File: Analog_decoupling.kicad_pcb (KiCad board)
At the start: 2 copper layers, 188.1 x 142 mm, 0 parts

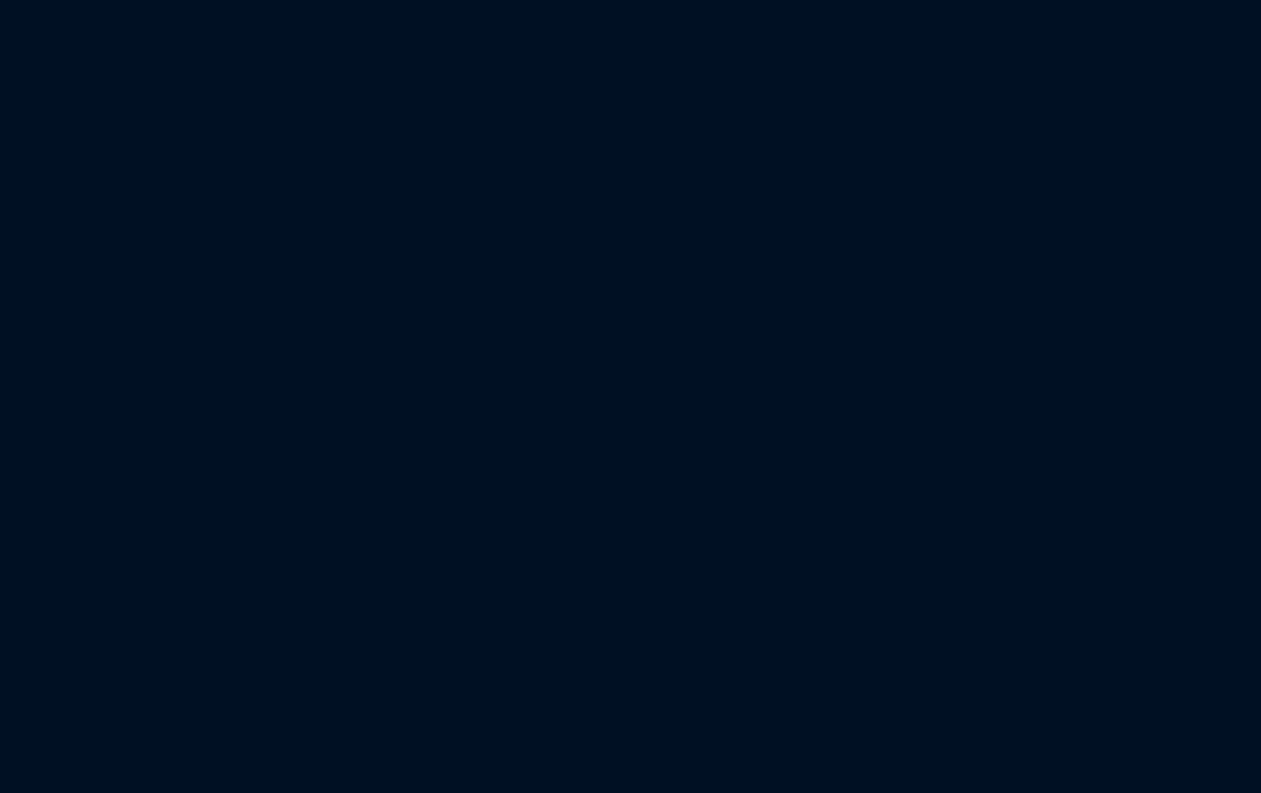
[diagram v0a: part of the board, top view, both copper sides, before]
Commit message: Analog decoupling elements place to PCB
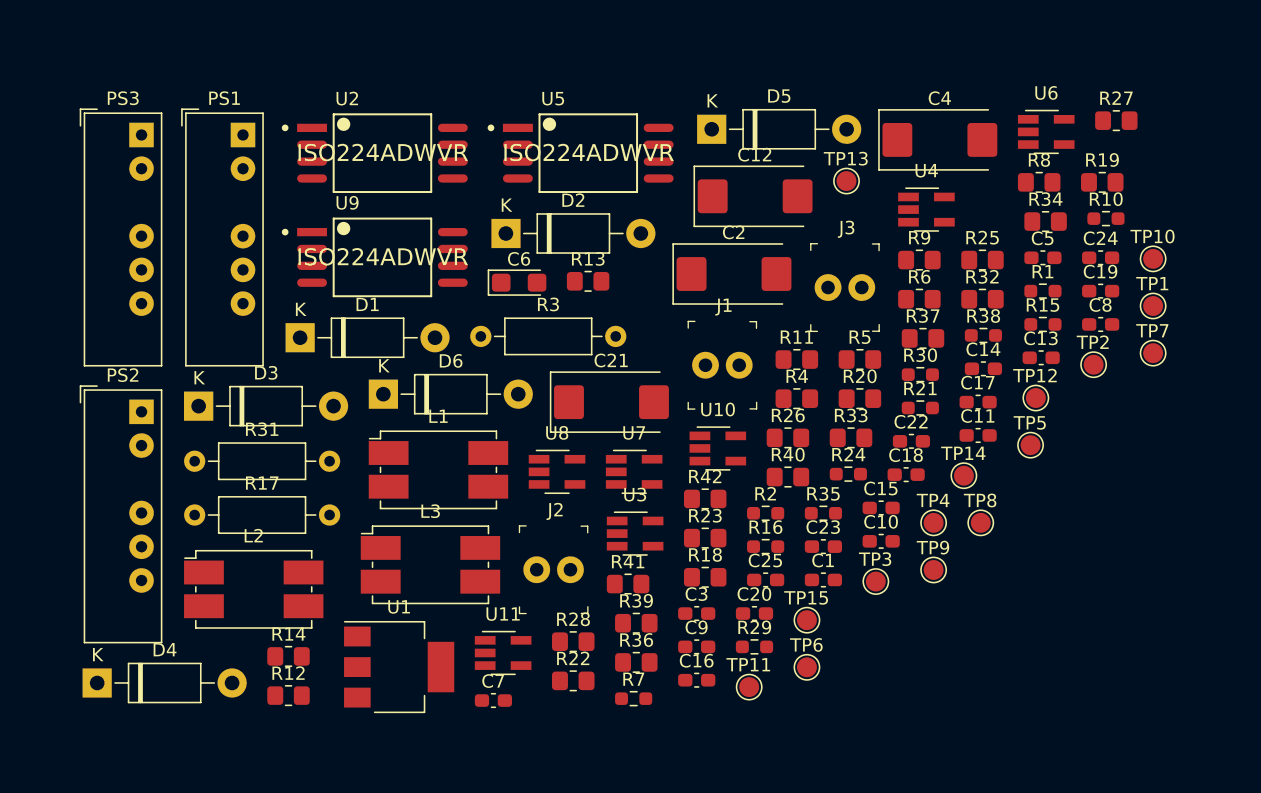
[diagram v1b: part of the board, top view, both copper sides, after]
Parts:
- added C1: 1µF, Capacitor_SMD:C_0603_1608Metric_Pad1.08x0.95mm_HandSolder, F.Cu at (167.9, 128.7)
- added C10: 1µF, Capacitor_SMD:C_0603_1608Metric_Pad1.08x0.95mm_HandSolder, F.Cu at (172.2, 125.8)
- added C11: 1µF, Capacitor_SMD:C_0603_1608Metric_Pad1.08x0.95mm_HandSolder, F.Cu at (179.5, 117.8)
- added C12: 10µFx35, Capacitor_Tantalum_SMD:CP_EIA-7343-30_AVX-N_Pad2.25x2.55mm_HandSolder, F.Cu at (162.7, 99.8)
- added C13: 1µF, Capacitor_SMD:C_0603_1608Metric_Pad1.08x0.95mm_HandSolder, F.Cu at (184.3, 112.0)
- added C14: 0.1µF, Capacitor_SMD:C_0603_1608Metric_Pad1.08x0.95mm_HandSolder, F.Cu at (179.9, 112.8)
- added C15: 0.22µF, Capacitor_SMD:C_0603_1608Metric_Pad1.08x0.95mm_HandSolder, F.Cu at (172.2, 123.3)
- added C16: 330pF, Capacitor_SMD:C_0603_1608Metric_Pad1.08x0.95mm_HandSolder, F.Cu at (158.3, 136.3)
- added C17: 1µF, Capacitor_SMD:C_0603_1608Metric_Pad1.08x0.95mm_HandSolder, F.Cu at (179.5, 115.3)
- added C18: 1µF, Capacitor_SMD:C_0603_1608Metric_Pad1.08x0.95mm_HandSolder, F.Cu at (174.1, 120.8)
- added C19: 1µF, Capacitor_SMD:C_0603_1608Metric_Pad1.08x0.95mm_HandSolder, F.Cu at (188.7, 107.0)
- added C2: 10µFx35, Capacitor_Tantalum_SMD:CP_EIA-7343-30_AVX-N_Pad2.25x2.55mm_HandSolder, F.Cu at (161.1, 105.7)
- added C20: 1µF, Capacitor_SMD:C_0603_1608Metric_Pad1.08x0.95mm_HandSolder, F.Cu at (162.7, 131.2)
- added C21: 10µFx35, Capacitor_Tantalum_SMD:CP_EIA-7343-30_AVX-N_Pad2.25x2.55mm_HandSolder, F.Cu at (151.9, 115.3)
- added C22: 1µF, Capacitor_SMD:C_0603_1608Metric_Pad1.08x0.95mm_HandSolder, F.Cu at (174.5, 118.3)
- added C23: 0.1µF, Capacitor_SMD:C_0603_1608Metric_Pad1.08x0.95mm_HandSolder, F.Cu at (167.9, 126.2)
- added C24: 0.22µF, Capacitor_SMD:C_0603_1608Metric_Pad1.08x0.95mm_HandSolder, F.Cu at (188.7, 104.5)
- added C25: 330pF, Capacitor_SMD:C_0603_1608Metric_Pad1.08x0.95mm_HandSolder, F.Cu at (163.5, 128.7)
- added C3: 1µF, Capacitor_SMD:C_0603_1608Metric_Pad1.08x0.95mm_HandSolder, F.Cu at (158.3, 131.2)
- added C4: 10µFx35, Capacitor_Tantalum_SMD:CP_EIA-7343-30_AVX-N_Pad2.25x2.55mm_HandSolder, F.Cu at (176.6, 95.6)
- added C5: 1µF, Capacitor_SMD:C_0603_1608Metric_Pad1.08x0.95mm_HandSolder, F.Cu at (184.4, 104.5)
- added C6: 10µFx16, Capacitor_Tantalum_SMD:CP_EIA-3216-10_Kemet-I, F.Cu at (144.9, 106.3)
- added C7: 0.1µF, Capacitor_SMD:C_0603_1608Metric_Pad1.08x0.95mm_HandSolder, F.Cu at (143.0, 137.8)
- added C8: 0.22µF, Capacitor_SMD:C_0603_1608Metric_Pad1.08x0.95mm_HandSolder, F.Cu at (188.7, 109.5)
- added C9: 330pF, Capacitor_SMD:C_0603_1608Metric_Pad1.08x0.95mm_HandSolder, F.Cu at (158.3, 133.8)
- added D1: 1N4743A, Diode_THT:D_DO-41_SOD81_P10.16mm_Horizontal, F.Cu at (128.4, 110.5)
- added D2: 1N4743A, Diode_THT:D_DO-41_SOD81_P10.16mm_Horizontal, F.Cu at (143.9, 102.6)
- added D3: 1N4743A, Diode_THT:D_DO-41_SOD81_P10.16mm_Horizontal, F.Cu at (120.8, 115.6)
- added D4: 1N4743A, Diode_THT:D_DO-41_SOD81_P10.16mm_Horizontal, F.Cu at (113.2, 136.5)
- added D5: 1N4743A, Diode_THT:D_DO-41_SOD81_P10.16mm_Horizontal, F.Cu at (159.4, 94.8)
- added D6: 1N4743A, Diode_THT:D_DO-41_SOD81_P10.16mm_Horizontal, F.Cu at (134.7, 114.7)
- added J1: 22-23-2021, digikey-footprints:PinHeader_1x2_P2.54mm_Drill1.02mm, F.Cu at (159.0, 112.5)
- added J2: 22-23-2021, digikey-footprints:PinHeader_1x2_P2.54mm_Drill1.02mm, F.Cu at (146.3, 127.9)
- added J3: 22-23-2021, digikey-footprints:PinHeader_1x2_P2.54mm_Drill1.02mm, F.Cu at (168.2, 106.7)
- added L1: B82790C0225N265, SVIELCOM:B82790C0225N265, F.Cu at (138.9, 120.4)
- added L2: B82790C0225N265, SVIELCOM:B82790C0225N265, F.Cu at (125.0, 129.4)
- added L3: B82790C0225N265, SVIELCOM:B82790C0225N265, F.Cu at (138.3, 127.6)
- added PS1: TMH2415S, Converter_DCDC:Converter_DCDC_XP_POWER-IAxxxxS_THT, F.Cu at (124.1, 95.2)
- added PS2: TMH2415S, Converter_DCDC:Converter_DCDC_XP_POWER-IAxxxxS_THT, F.Cu at (116.5, 116.1)
- added PS3: TMH2415S, Converter_DCDC:Converter_DCDC_XP_POWER-IAxxxxS_THT, F.Cu at (116.5, 95.2)
- added R1: 3.3K, Resistor_SMD:R_0603_1608Metric_Pad0.98x0.95mm_HandSolder, F.Cu at (184.4, 107.0)
- added R10: 3.3K, Resistor_SMD:R_0603_1608Metric_Pad0.98x0.95mm_HandSolder, F.Cu at (189.1, 101.5)
- added R11: 2K, Resistor_SMD:R_0805_2012Metric_Pad1.20x1.40mm_HandSolder, F.Cu at (165.9, 112.1)
- added R12: 1K, Resistor_SMD:R_0805_2012Metric_Pad1.20x1.40mm_HandSolder, F.Cu at (127.6, 137.4)
- added R13: 1K, Resistor_SMD:R_0805_2012Metric_Pad1.20x1.40mm_HandSolder, F.Cu at (150.1, 106.2)
- added R14: 1K, Resistor_SMD:R_0805_2012Metric_Pad1.20x1.40mm_HandSolder, F.Cu at (127.6, 134.5)
- added R15: 3.3K, Resistor_SMD:R_0603_1608Metric_Pad0.98x0.95mm_HandSolder, F.Cu at (184.4, 109.5)
- added R16: 825, Resistor_SMD:R_0603_1608Metric_Pad0.98x0.95mm_HandSolder, F.Cu at (163.5, 126.2)
- added R17: 1K, Resistor_THT:R_Axial_DIN0207_L6.3mm_D2.5mm_P10.16mm_Horizontal, F.Cu at (120.5, 123.8)
- added R18: 10K, Resistor_SMD:R_0805_2012Metric_Pad1.20x1.40mm_HandSolder, F.Cu at (159.0, 128.5)
- added R19: 1.1K, Resistor_SMD:R_0805_2012Metric_Pad1.20x1.40mm_HandSolder, F.Cu at (188.9, 98.8)
- added R2: 825, Resistor_SMD:R_0603_1608Metric_Pad0.98x0.95mm_HandSolder, F.Cu at (163.5, 123.7)
- added R20: 10K, Resistor_SMD:R_0805_2012Metric_Pad1.20x1.40mm_HandSolder, F.Cu at (170.6, 115.1)
- added R21: 825, Resistor_SMD:R_0603_1608Metric_Pad0.98x0.95mm_HandSolder, F.Cu at (175.2, 115.8)
- added R22: 10K, Resistor_SMD:R_0805_2012Metric_Pad1.20x1.40mm_HandSolder, F.Cu at (149.0, 136.3)
- added R23: 10K, Resistor_SMD:R_0805_2012Metric_Pad1.20x1.40mm_HandSolder, F.Cu at (159.0, 125.6)
- added R24: 3.3K, Resistor_SMD:R_0603_1608Metric_Pad0.98x0.95mm_HandSolder, F.Cu at (169.7, 120.7)
- added R25: 2K, Resistor_SMD:R_0805_2012Metric_Pad1.20x1.40mm_HandSolder, F.Cu at (179.8, 104.6)
- added R26: 1K, Resistor_SMD:R_0805_2012Metric_Pad1.20x1.40mm_HandSolder, F.Cu at (165.2, 118.0)
- added R27: 1K, Resistor_SMD:R_0805_2012Metric_Pad1.20x1.40mm_HandSolder, F.Cu at (189.9, 94.1)
- added R28: 1K, Resistor_SMD:R_0805_2012Metric_Pad1.20x1.40mm_HandSolder, F.Cu at (149.0, 133.4)
- added R29: 3.3K, Resistor_SMD:R_0603_1608Metric_Pad0.98x0.95mm_HandSolder, F.Cu at (162.7, 133.8)
- added R3: 1K, Resistor_THT:R_Axial_DIN0207_L6.3mm_D2.5mm_P10.16mm_Horizontal, F.Cu at (142.1, 110.4)
- added R30: 825, Resistor_SMD:R_0603_1608Metric_Pad0.98x0.95mm_HandSolder, F.Cu at (175.2, 113.3)
- added R31: 1K, Resistor_THT:R_Axial_DIN0207_L6.3mm_D2.5mm_P10.16mm_Horizontal, F.Cu at (120.5, 119.8)
- added R32: 10K, Resistor_SMD:R_0805_2012Metric_Pad1.20x1.40mm_HandSolder, F.Cu at (179.8, 107.6)
- added R33: 1.1K, Resistor_SMD:R_0805_2012Metric_Pad1.20x1.40mm_HandSolder, F.Cu at (169.9, 118.0)
- added R34: 10K, Resistor_SMD:R_0805_2012Metric_Pad1.20x1.40mm_HandSolder, F.Cu at (184.6, 101.7)
- added R35: 825, Resistor_SMD:R_0603_1608Metric_Pad0.98x0.95mm_HandSolder, F.Cu at (167.9, 123.7)
- added R36: 10K, Resistor_SMD:R_0805_2012Metric_Pad1.20x1.40mm_HandSolder, F.Cu at (153.8, 134.9)
- added R37: 10K, Resistor_SMD:R_0805_2012Metric_Pad1.20x1.40mm_HandSolder, F.Cu at (175.4, 110.5)
- added R38: 3.3K, Resistor_SMD:R_0603_1608Metric_Pad0.98x0.95mm_HandSolder, F.Cu at (179.9, 110.3)
- added R39: 2K, Resistor_SMD:R_0805_2012Metric_Pad1.20x1.40mm_HandSolder, F.Cu at (153.8, 132.0)
- added R4: 10K, Resistor_SMD:R_0805_2012Metric_Pad1.20x1.40mm_HandSolder, F.Cu at (165.9, 115.1)
- added R40: 1K, Resistor_SMD:R_0805_2012Metric_Pad1.20x1.40mm_HandSolder, F.Cu at (165.2, 121.0)
- added R41: 1K, Resistor_SMD:R_0805_2012Metric_Pad1.20x1.40mm_HandSolder, F.Cu at (153.1, 129.0)
- added R42: 1K, Resistor_SMD:R_0805_2012Metric_Pad1.20x1.40mm_HandSolder, F.Cu at (159.0, 122.6)
- added R5: 1.1K, Resistor_SMD:R_0805_2012Metric_Pad1.20x1.40mm_HandSolder, F.Cu at (170.6, 112.1)
- added R6: 10K, Resistor_SMD:R_0805_2012Metric_Pad1.20x1.40mm_HandSolder, F.Cu at (175.1, 107.6)
- added R7: 825, Resistor_SMD:R_0603_1608Metric_Pad0.98x0.95mm_HandSolder, F.Cu at (153.6, 137.7)
- added R8: 10K, Resistor_SMD:R_0805_2012Metric_Pad1.20x1.40mm_HandSolder, F.Cu at (184.1, 98.8)
- added R9: 10K, Resistor_SMD:R_0805_2012Metric_Pad1.20x1.40mm_HandSolder, F.Cu at (175.1, 104.6)
- added TP1: TestPoint, TestPoint:TestPoint_Pad_D1.5mm, F.Cu at (192.7, 108.1)
- added TP10: TestPoint, TestPoint:TestPoint_Pad_D1.5mm, F.Cu at (192.7, 104.5)
- added TP11: TestPoint, TestPoint:TestPoint_Pad_D1.5mm, F.Cu at (162.3, 136.8)
- added TP12: TestPoint, TestPoint:TestPoint_Pad_D1.5mm, F.Cu at (183.9, 115.0)
- added TP13: TestPoint, TestPoint:TestPoint_Pad_D1.5mm, F.Cu at (169.6, 98.7)
- added TP14: TestPoint, TestPoint:TestPoint_Pad_D1.5mm, F.Cu at (178.4, 120.9)
- added TP15: TestPoint, TestPoint:TestPoint_Pad_D1.5mm, F.Cu at (166.6, 131.7)
- added TP2: TestPoint, TestPoint:TestPoint_Pad_D1.5mm, F.Cu at (188.2, 112.5)
- added TP3: TestPoint, TestPoint:TestPoint_Pad_D1.5mm, F.Cu at (171.8, 128.8)
- added TP4: TestPoint, TestPoint:TestPoint_Pad_D1.5mm, F.Cu at (176.2, 124.4)
- added TP5: TestPoint, TestPoint:TestPoint_Pad_D1.5mm, F.Cu at (183.5, 118.6)
- added TP6: TestPoint, TestPoint:TestPoint_Pad_D1.5mm, F.Cu at (166.6, 135.3)
- added TP7: TestPoint, TestPoint:TestPoint_Pad_D1.5mm, F.Cu at (192.7, 111.6)
- added TP8: TestPoint, TestPoint:TestPoint_Pad_D1.5mm, F.Cu at (179.7, 124.4)
- added TP9: TestPoint, TestPoint:TestPoint_Pad_D1.5mm, F.Cu at (176.2, 128.0)
- added U1: LT1129CST-5#PBF, Package_TO_SOT_SMD:SOT-223-3_TabPin2, F.Cu at (135.9, 135.3)
- added U10: TLV9001IDBVR, Package_TO_SOT_SMD:SOT-23-5_HandSoldering, F.Cu at (159.9, 118.8)
- added U11: TLV9001IDBVR, Package_TO_SOT_SMD:SOT-23-5_HandSoldering, F.Cu at (143.7, 134.2)
- added U2: ISO224ADWVR, SVIELCOM:Texas_Instruments-DWV0008A-0-0-IPC_A, F.Cu at (134.6, 96.6)
- added U3: TLV9001IDBVR, Package_TO_SOT_SMD:SOT-23-5_HandSoldering, F.Cu at (153.7, 125.2)
- added U4: TLV9001IDBVR, Package_TO_SOT_SMD:SOT-23-5_HandSoldering, F.Cu at (175.6, 100.8)
- added U5: ISO224ADWVR, SVIELCOM:Texas_Instruments-DWV0008A-0-0-IPC_A, F.Cu at (150.1, 96.6)
- added U6: TLV9001IDBVR, Package_TO_SOT_SMD:SOT-23-5_HandSoldering, F.Cu at (184.6, 95.0)
- added U7: TLV9001IDBVR, Package_TO_SOT_SMD:SOT-23-5_HandSoldering, F.Cu at (153.6, 120.6)
- added U8: REF1933AIDDCT, Package_TO_SOT_SMD:SOT-23-5_HandSoldering, F.Cu at (147.8, 120.6)
- added U9: ISO224ADWVR, SVIELCOM:Texas_Instruments-DWV0008A-0-0-IPC_A, F.Cu at (134.6, 104.4)

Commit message: main PCB changes
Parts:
- added J4: 302-S101, digikey-footprints:PinHeader_2x5_P2.54mm_Drill1.2mm, F.Cu at (230.3, 172.8)
- added J5: OSTTC020162, digikey-footprints:Term_Block_1x2_P5mm, F.Cu at (153.4, 77.3)
- moved U9 79.7 mm to (193.9, 157.8)
- moved U1 77.0 mm to (179.7, 72.0)
- moved U5 72.3 mm to (79.6, 112.5)
- moved L3 68.7 mm to (194.6, 166.9)
- moved L1 64.6 mm to (80.4, 92.8)
- moved U2 57.3 mm to (144.5, 153.1)
- moved PS2 43.5 mm to (73.8, 124.7)
- moved L2 41.1 mm to (144.0, 165.9)
- moved PS1 40.6 mm to (144.0, 59.8)
- moved PS3 37.1 mm to (122.0, 58.5)
- moved TP2 18.5 mm to (204.3, 103.5)
- moved C8 18.1 mm to (203.9, 99.5)

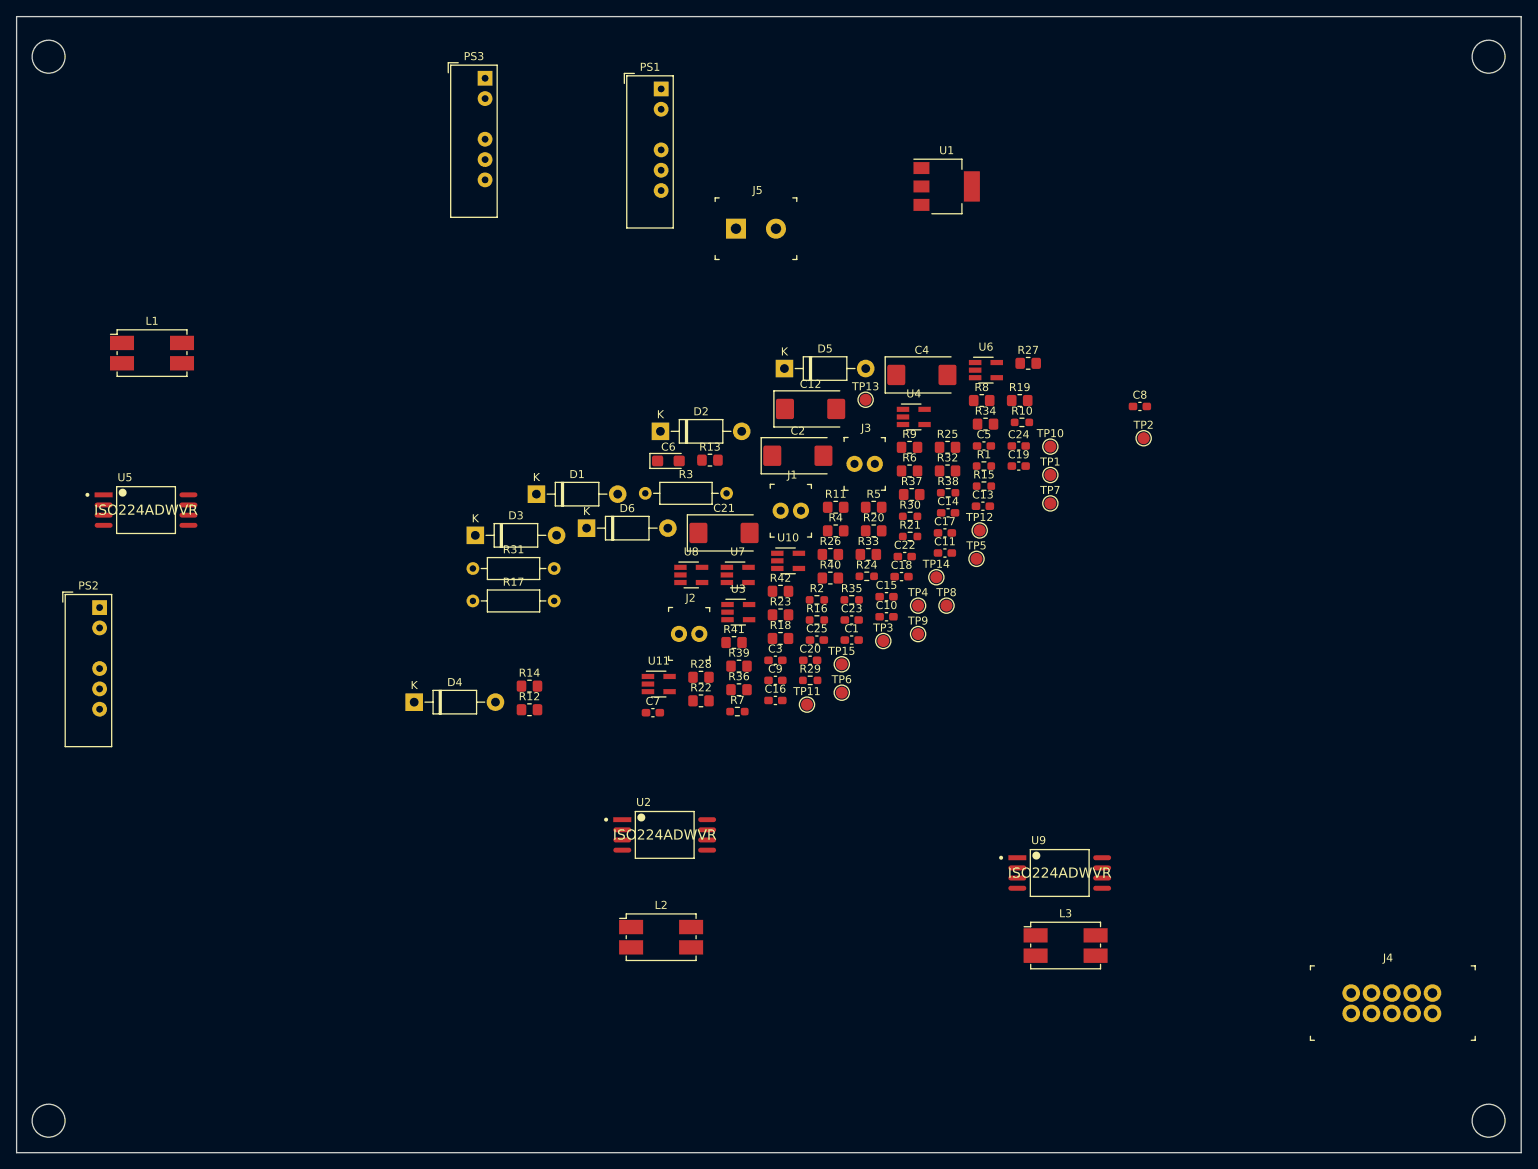
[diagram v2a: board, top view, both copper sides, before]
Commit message: Analog decoupling PCB layout done. Order sent to manufacturer
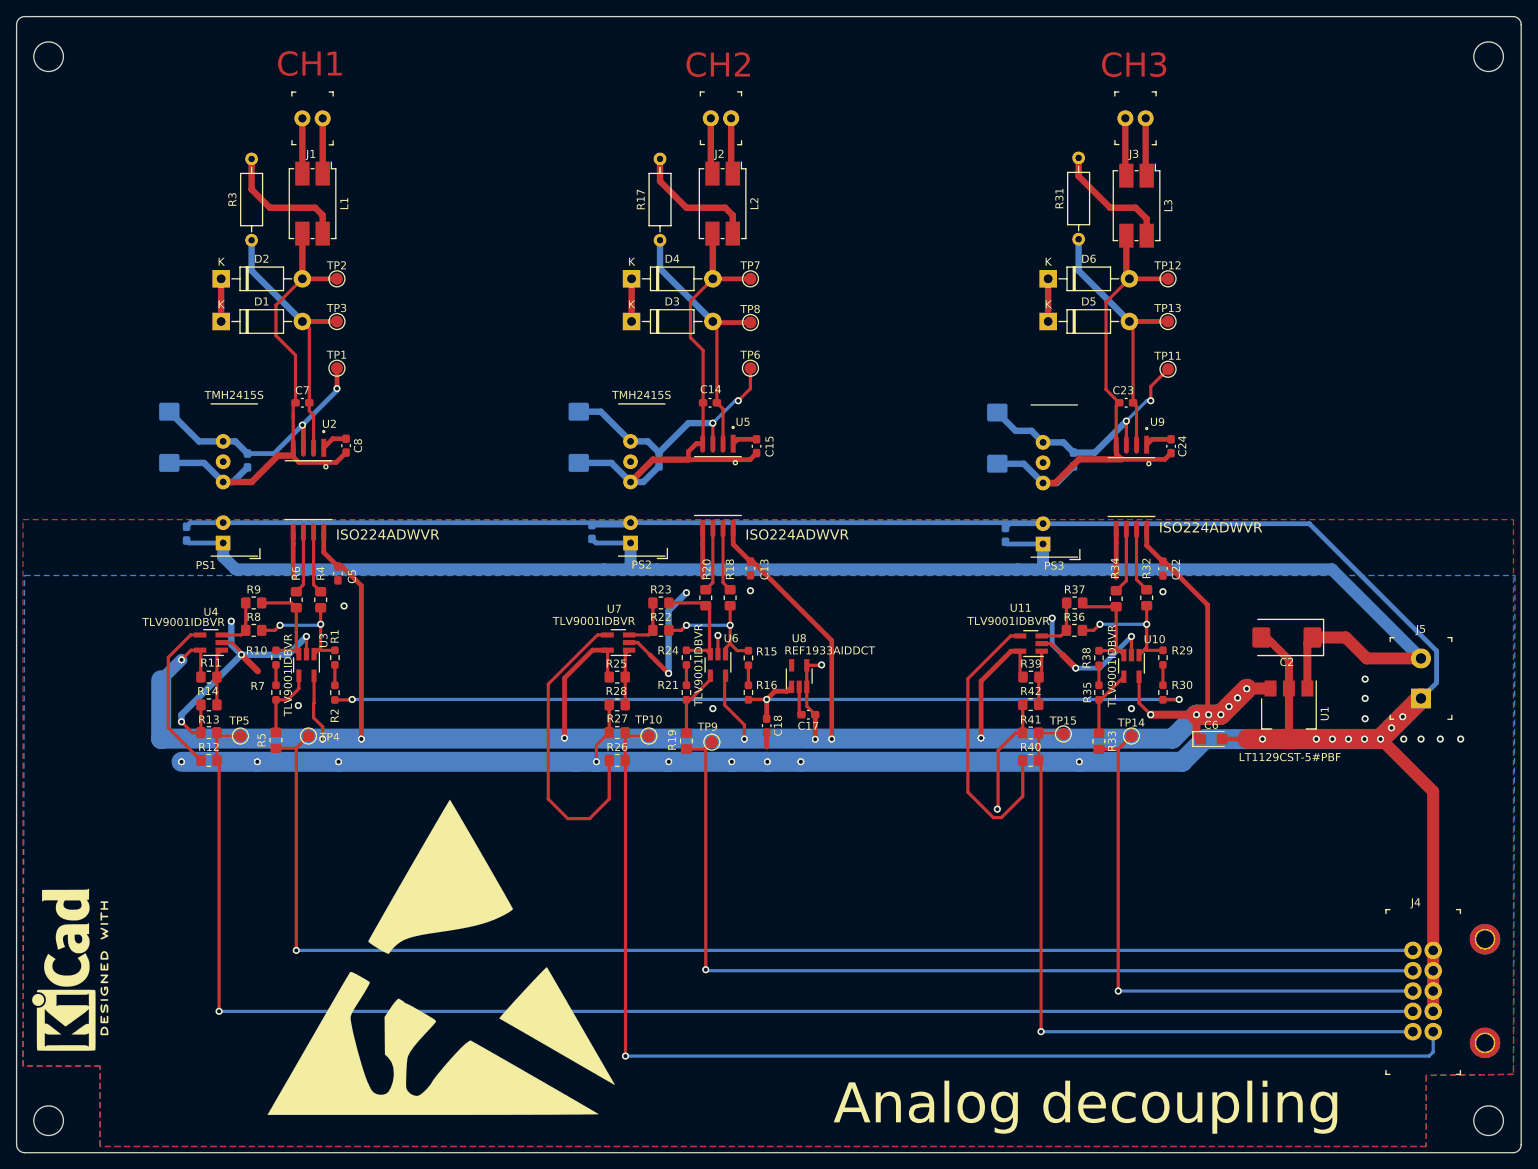
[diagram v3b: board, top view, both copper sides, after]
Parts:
- removed C16, C25, C9: 330pF, Capacitor_SMD:C_0603_1608Metric_Pad1.08x0.95mm_HandSolder
- added REF**: MountingHole_2.1mm, MountingHole:MountingHole_2.1mm, F.Cu at (198.9, 111.6)
- added REF**: MountingHole_3.7mm, MountingHole:MountingHole_3.7mm, F.Cu at (247.5, 188.8)
- added REF**: MountingHole_3.7mm, MountingHole:MountingHole_3.7mm, F.Cu at (247.5, 55.8)
- added REF**: MountingHole_2.1mm, MountingHole:MountingHole_2.1mm, F.Cu at (147.3, 111.5)
- added REF**: MountingHole_2.1mm, MountingHole:MountingHole_2.1mm, F.Cu at (96.4, 111.5)
- added REF**: KiCad-Logo2_8mm_SilkScreen, Symbol:KiCad-Logo2_8mm_SilkScreen, F.Cu at (69.3, 169.9)
- added REF**: ESD-Logo_44.1x40mm_SilkScreen, Symbol:ESD-Logo_44.1x40mm_SilkScreen, F.Cu at (116.6, 168.3)
- added REF**: MountingHole_2.2mm_M2_DIN965_Pad_TopBottom, MountingHole:MountingHole_2.2mm_M2_DIN965_Pad_TopBottom, F.Cu at (247.0, 166.1)
- added REF**: MountingHole_2.2mm_M2_DIN965_Pad_TopBottom, MountingHole:MountingHole_2.2mm_M2_DIN965_Pad_TopBottom, F.Cu at (247.0, 179.1)
- added REF**: MountingHole_3.7mm, MountingHole:MountingHole_3.7mm, F.Cu at (67.5, 55.8)
- added REF**: MountingHole_3.7mm, MountingHole:MountingHole_3.7mm, F.Cu at (67.5, 188.8)
- C1, C10, C11, C12, C19, C20, C21, C3, C4: moved to B.Cu
- PS3: value TMH2415S -> (none)
- moved J5 103.8 mm to (239.0, 136.0), turned to 90 degrees
- moved TP2 102.8 mm to (103.5, 83.6)
- moved C8 99.3 mm to (104.6, 104.4), turned to 270 degrees
- moved R10 97.8 mm to (95.9, 130.9), turned to 270 degrees
- moved R8 95.4 mm to (93.1, 127.5)
- moved TP5 94.6 mm to (91.4, 140.7)
- moved C4 94.4 mm to (82.5, 103.4), turned to 270 degrees
- moved L3 92.9 mm to (203.5, 74.4), turned to 270 degrees
- moved U4 92.3 mm to (87.8, 129.0), turned to 180 degrees
- moved L2 92.0 mm to (151.7, 74.2), turned to 270 degrees
- moved PS3 90.9 mm to (191.8, 116.7), turned to 180 degrees
- moved TP1 90.2 mm to (103.5, 94.7)
- moved R31 86.2 mm to (196.2, 78.6), turned to 90 degrees
- moved R1 84.6 mm to (103.3, 130.9), turned to 270 degrees
- moved R9 84.2 mm to (93.1, 124.1)
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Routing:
- net GNDREF: track 0.00 -> 546.0 mm, vias 0 -> 41
- net +5V_Analog: track 0.00 -> 330.9 mm, vias 0 -> 16
- net +24V: track 0.00 -> 199.4 mm
- net /A_CH1_FAULT: track 0.00 -> 187.9 mm, vias 0 -> 1
- net /ADC1_P: track 0.00 -> 169.5 mm, vias 0 -> 1
- net /A_CH2_FAULT: track 0.00 -> 147.3 mm, vias 0 -> 1
- net /ADC2_P: track 0.00 -> 119.7 mm, vias 0 -> 1
- net /Ref_1,65V: track 0.00 -> 116.1 mm, vias 0 -> 3
- net /A_CH3_FAULT: track 0.00 -> 87.1 mm, vias 0 -> 1
- net /ADC3_P: track 0.00 -> 71.8 mm, vias 0 -> 1
- net Net-(C11-Pad2): track 0.00 -> 65.1 mm
- net Net-(C3-Pad2): track 0.00 -> 64.4 mm
- net Net-(C20-Pad2): track 0.00 -> 64.4 mm
- net Net-(R26-Pad1): track 0.00 -> 39.6 mm
- net Net-(R40-Pad1): track 0.00 -> 36.7 mm
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- added copper zone on B.Cu, net GNDREF
- added copper zone on F.Cu, net GNDREF
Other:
- outline, holes or cut-outs redrawn
- net class Default: clearance 0.2 -> 0.4; via_dia 0.6 -> 0.7
- net class Power: clearance 0.2 -> 0.4; via_dia 0.7 -> 0.9; via_drill 0.4 -> 0.5
- rule pad_to_mask_clearance: 0 -> 0.051
- rule trace_clearance: 0.2 -> 0.4
- board text added: "Analog decoupling"
- board text added: "CH1"
- board text added: "CH2"
- board text added: "CH3"
- board text added: "Schema and PCB designed by SVIELCOM"
